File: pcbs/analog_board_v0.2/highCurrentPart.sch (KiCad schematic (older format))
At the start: 36 parts, among them J3 CONN_01X04, P1 CONN_01X03, P2 CONN_01X03, P3 CONN_01X03, Q1 DMP2035U, Q2 TSM2314, Q3 DMP2035U, Q4 TSM2314, Q5 DMP2035U, Q6 TSM2314, Q7 DMP2035U, Q8 TSM2314, Q9 MMBT3904, U3 ICL7660S, U4 AD8616

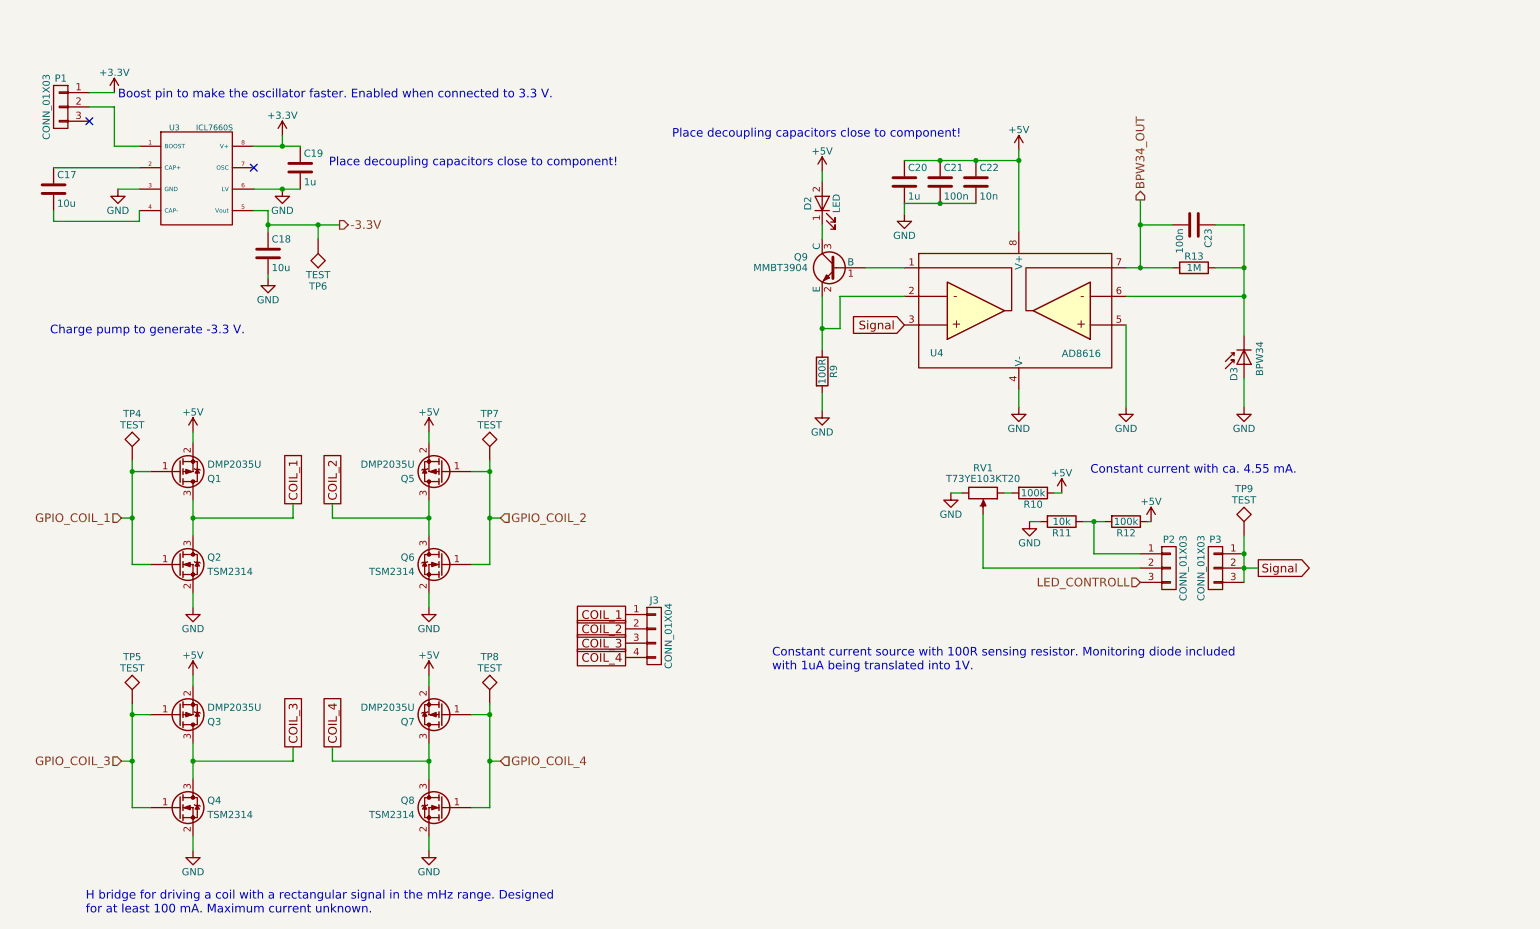
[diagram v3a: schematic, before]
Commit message: Small changes on the backplane standing out.
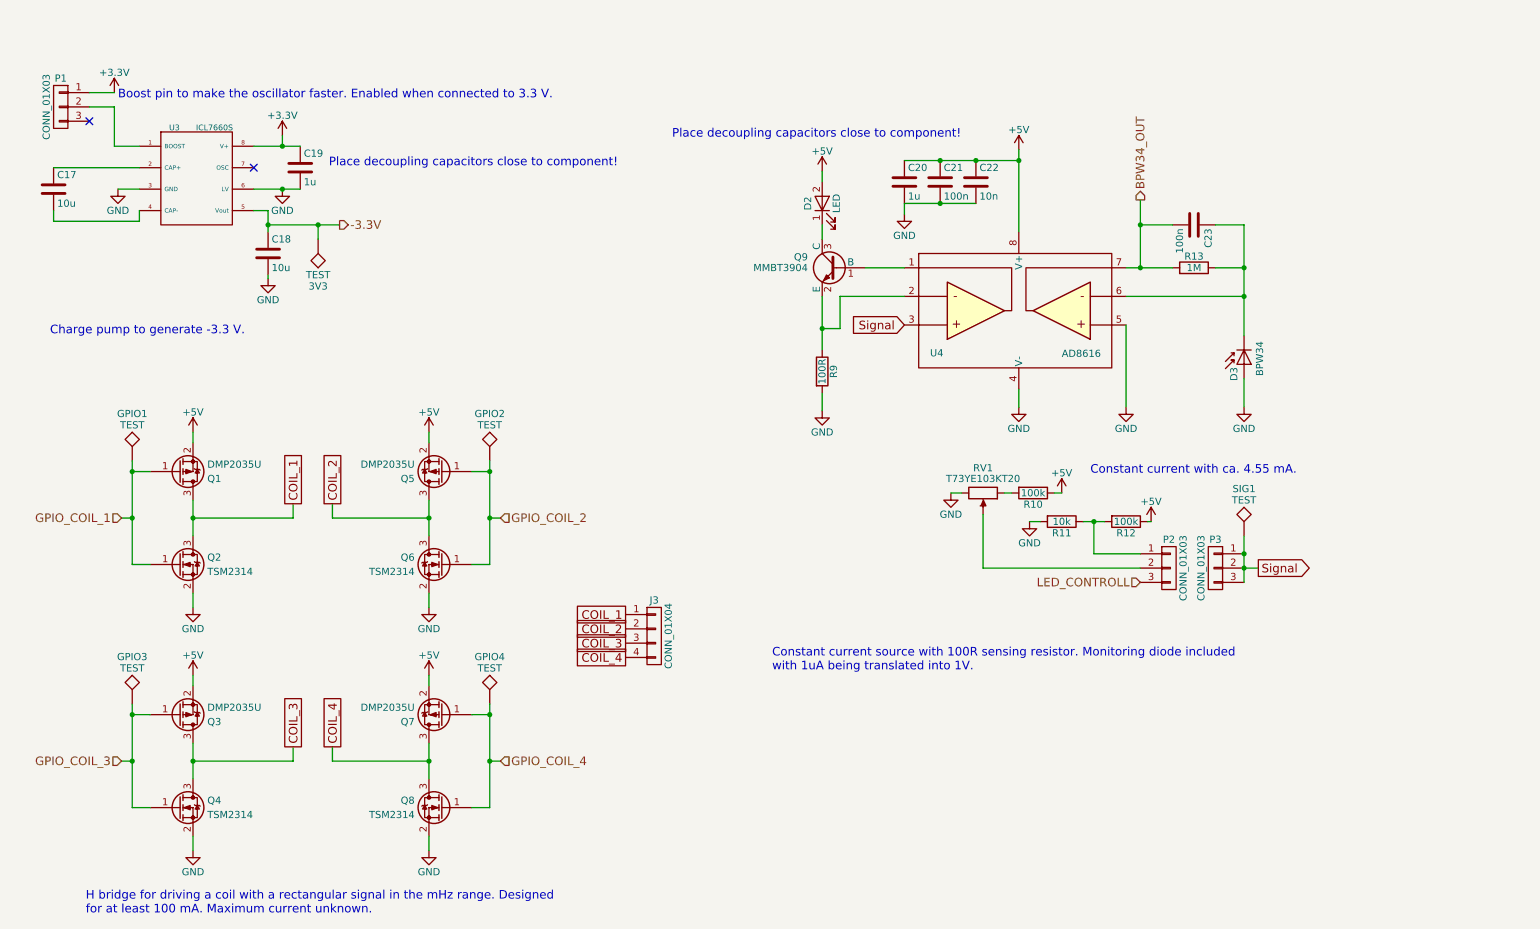
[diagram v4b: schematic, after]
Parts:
- renumbered TP6 to 3V3, TP4 to GPIO1, TP7 to GPIO2, TP5 to GPIO3, TP8 to GPIO4, TP9 to SIG1
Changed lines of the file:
@@
 $EndDescr
 $Comp
-L GND #PWR36
+L GND #PWR018
 U 1 1 5940A4E3
 P 8150 3325
-F 0 "#PWR36" H 8150 3075 50  0001 C CNN
+F 0 "#PWR018" H 8150 3075 50  0001 C CNN
 F 1 "GND" H 8150 3175 50  0000 C CNN
 F 2 "" H 8150 3325 50  0000 C CNN
@@
 $EndComp
 $Comp
-L GND #PWR41
+L GND #PWR019
 U 1 1 5940A554
 P 9725 3325
-F 0 "#PWR41" H 9725 3075 50  0001 C CNN
+F 0 "#PWR019" H 9725 3075 50  0001 C CNN
 F 1 "GND" H 9725 3175 50  0000 C CNN
 F 2 "" H 9725 3325 50  0000 C CNN
@@
 	6775 2050 6775 2150
 $Comp
-L +5V #PWR31
+L +5V #PWR020
 U 1 1 5940A5DC
 P 6775 1675
-F 0 "#PWR31" H 6775 1525 50  0001 C CNN
+F 0 "#PWR020" H 6775 1525 50  0001 C CNN
 F 1 "+5V" H 6775 1815 50  0000 C CNN
 F 2 "" H 6775 1675 50  0000 C CNN
@@
 	6775 1675 6775 1750
 $Comp
-L GND #PWR32
+L GND #PWR021
 U 1 1 5940A5E4
 P 6775 3350
-F 0 "#PWR32" H 6775 3100 50  0001 C CNN
+F 0 "#PWR021" H 6775 3100 50  0001 C CNN
 F 1 "GND" H 6775 3200 50  0000 C CNN
 F 2 "" H 6775 3350 50  0000 C CNN
@@
 Signal
 $Comp
-L GND #PWR34
+L GND #PWR022
 U 1 1 5940A601
 P 7675 3925
-F 0 "#PWR34" H 7675 3675 50  0001 C CNN
+F 0 "#PWR022" H 7675 3675 50  0001 C CNN
 F 1 "GND" H 7675 3775 50  0000 C CNN
 F 2 "" H 7675 3925 50  0000 C CNN
@@
 Signal
 $Comp
-L +5V #PWR38
+L +5V #PWR023
 U 1 1 5940A60A
 P 8450 3925
-F 0 "#PWR38" H 8450 3775 50  0001 C CNN
+F 0 "#PWR023" H 8450 3775 50  0001 C CNN
 F 1 "+5V" H 8450 4065 50  0000 C CNN
 F 2 "" H 8450 3925 50  0000 C CNN
@@
 Connection ~ 6775 2775
 $Comp
-L GND #PWR39
+L GND #PWR024
 U 1 1 5940EF10
 P 8900 3325
-F 0 "#PWR39" H 8900 3075 50  0001 C CNN
+F 0 "#PWR024" H 8900 3075 50  0001 C CNN
 F 1 "GND" H 8900 3175 50  0000 C CNN
 F 2 "" H 8900 3325 50  0000 C CNN
@@
 	8900 2750 8900 3325
 $Comp
-L +5V #PWR35
+L +5V #PWR025
 U 1 1 594122D1
 P 8150 1525
-F 0 "#PWR35" H 8150 1375 50  0001 C CNN
+F 0 "#PWR025" H 8150 1375 50  0001 C CNN
 F 1 "+5V" H 8150 1665 50  0000 C CNN
 F 2 "" H 8150 1525 50  0000 C CNN
@@
 Connection ~ 7600 1600
 $Comp
-L GND #PWR33
+L GND #PWR026
 U 1 1 594122F3
 P 7350 1975
-F 0 "#PWR33" H 7350 1725 50  0001 C CNN
+F 0 "#PWR026" H 7350 1725 50  0001 C CNN
 F 1 "GND" H 7350 1825 50  0000 C CNN
 F 2 "" H 7350 1975 50  0000 C CNN
@@
 	9725 4450 9825 4450
 $Comp
-L TEST TP9
+L TEST SIG1
 U 1 1 594174AB
 P 9725 4225
-F 0 "TP9" H 9725 4525 50  0000 C BNN
+F 0 "SIG1" H 9725 4525 50  0000 C BNN
 F 1 "TEST" H 9725 4475 50  0000 C CNN
 F 2 "Tespoints:TP_SMD_quadr_1mm" H 9725 4225 50  0001 C CNN
@@
 $EndComp
 $Comp
-L +5V #PWR40
+L +5V #PWR027
 U 1 1 5941842E
 P 9075 4125
-F 0 "#PWR40" H 9075 3975 50  0001 C CNN
+F 0 "#PWR027" H 9075 3975 50  0001 C CNN
 F 1 "+5V" H 9075 4265 50  0000 C CNN
 F 2 "" H 9075 4125 50  0000 C CNN
@@
 	8600 4125 8750 4125
 $Comp
-L GND #PWR37
+L GND #PWR028
 U 1 1 5941869D
 P 8225 4125
-F 0 "#PWR37" H 8225 3875 50  0001 C CNN
+F 0 "#PWR028" H 8225 3875 50  0001 C CNN
 F 1 "GND" H 8225 3975 50  0000 C CNN
 F 2 "" H 8225 4125 50  0000 C CNN
@@
 BPW34_OUT
 $Comp
-L GND #PWR26
+L GND #PWR029
 U 1 1 59553CC6
 P 3000 1800
-F 0 "#PWR26" H 3000 1550 50  0001 C CNN
+F 0 "#PWR029" H 3000 1550 50  0001 C CNN
 F 1 "GND" H 3000 1650 50  0000 C CNN
 F 2 "" H 3000 1800 50  0001 C CNN
@@
 	2375 5675 2375 5925
 $Comp
-L GND #PWR23
+L GND #PWR030
 U 1 1 59557860
 P 2375 6425
-F 0 "#PWR23" H 2375 6175 50  0001 C CNN
+F 0 "#PWR030" H 2375 6175 50  0001 C CNN
 F 1 "GND" H 2375 6275 50  0000 C CNN
 F 2 "" H 2375 6425 50  0000 C CNN
@@
 	2375 6325 2375 6425
 $Comp
-L +5V #PWR22
+L +5V #PWR031
 U 1 1 59557DF9
 P 2375 5200
-F 0 "#PWR22" H 2375 5050 50  0001 C CNN
+F 0 "#PWR031" H 2375 5050 50  0001 C CNN
 F 1 "+5V" H 2375 5340 50  0000 C CNN
 F 2 "" H 2375 5200 50  0000 C CNN
@@
 	4025 5675 4025 5925
 $Comp
-L GND #PWR30
+L GND #PWR032
 U 1 1 59558304
 P 4025 6425
-F 0 "#PWR30" H 4025 6175 50  0001 C CNN
+F 0 "#PWR032" H 4025 6175 50  0001 C CNN
 F 1 "GND" H 4025 6275 50  0000 C CNN
 F 2 "" H 4025 6425 50  0000 C CNN
@@
 	4025 6325 4025 6425
 $Comp
-L +5V #PWR29
+L +5V #PWR033
 U 1 1 5955830B
 P 4025 5200
-F 0 "#PWR29" H 4025 5050 50  0001 C CNN
+F 0 "#PWR033" H 4025 5050 50  0001 C CNN
 F 1 "+5V" H 4025 5340 50  0000 C CNN
 F 2 "" H 4025 5200 50  0000 C CNN
@@
 	2375 3975 2375 4225
 $Comp
-L GND #PWR21
+L GND #PWR034
 U 1 1 5956291A
 P 2375 4725
-F 0 "#PWR21" H 2375 4475 50  0001 C CNN
+F 0 "#PWR034" H 2375 4475 50  0001 C CNN
 F 1 "GND" H 2375 4575 50  0000 C CNN
 F 2 "" H 2375 4725 50  0000 C CNN
@@
 	2375 4625 2375 4725
 $Comp
-L +5V #PWR20
+L +5V #PWR035
 U 1 1 59562921
 P 2375 3500
-F 0 "#PWR20" H 2375 3350 50  0001 C CNN
+F 0 "#PWR035" H 2375 3350 50  0001 C CNN
 F 1 "+5V" H 2375 3640 50  0000 C CNN
 F 2 "" H 2375 3500 50  0000 C CNN
@@
 	4025 3975 4025 4225
 $Comp
-L GND #PWR28
+L GND #PWR036
 U 1 1 59562931
 P 4025 4725
-F 0 "#PWR28" H 4025 4475 50  0001 C CNN
+F 0 "#PWR036" H 4025 4475 50  0001 C CNN
 F 1 "GND" H 4025 4575 50  0000 C CNN
 F 2 "" H 4025 4725 50  0000 C CNN
@@
 	4025 4625 4025 4725
 $Comp
-L +5V #PWR27
+L +5V #PWR037
 U 1 1 59562938
 P 4025 3500
-F 0 "#PWR27" H 4025 3350 50  0001 C CNN
+F 0 "#PWR037" H 4025 3350 50  0001 C CNN
 F 1 "+5V" H 4025 3640 50  0000 C CNN
 F 2 "" H 4025 3500 50  0000 C CNN
@@
 LED_CONTROLL
 $Comp
-L GND #PWR19
+L GND #PWR038
 U 1 1 59563916
 P 1850 1800
-F 0 "#PWR19" H 1850 1550 50  0001 C CNN
+F 0 "#PWR038" H 1850 1550 50  0001 C CNN
 F 1 "GND" H 1850 1650 50  0000 C CNN
 F 2 "" H 1850 1800 50  0001 C CNN
@@
 	2000 2025 2000 1950
 $Comp
-L +3.3V #PWR25
+L +3.3V #PWR039
 U 1 1 59563EC0
 P 3000 1425
-F 0 "#PWR25" H 3000 1275 50  0001 C CNN
+F 0 "#PWR039" H 3000 1275 50  0001 C CNN
 F 1 "+3.3V" H 3000 1565 50  0000 C CNN
 F 2 "" H 3000 1425 50  0001 C CNN
@@
 	2900 1950 2900 2100
 $Comp
-L GND #PWR24
+L GND #PWR040
 U 1 1 5956469D
 P 2900 2425
-F 0 "#PWR24" H 2900 2175 50  0001 C CNN
+F 0 "#PWR040" H 2900 2175 50  0001 C CNN
 F 1 "GND" H 2900 2275 50  0000 C CNN
 F 2 "" H 2900 2425 50  0001 C CNN
@@
 $EndComp
 $Comp
-L +3.3V #PWR18
+L +3.3V #PWR041
 U 1 1 595680C2
 P 1825 1125
-F 0 "#PWR18" H 1825 975 50  0001 C CNN
+F 0 "#PWR041" H 1825 975 50  0001 C CNN
 F 1 "+3.3V" H 1825 1265 50  0000 C CNN
 F 2 "" H 1825 1125 50  0001 C CNN
@@
 COIL_4
 $Comp
-L TEST TP4
+L TEST GPIO1
 U 1 1 59595C55
 P 1950 3700
-F 0 "TP4" H 1950 4000 50  0000 C BNN
+F 0 "GPIO1" H 1950 4000 50  0000 C BNN
 F 1 "TEST" H 1950 3950 50  0000 C CNN
 F 2 "Tespoints:TP_SMD_quadr_1mm" H 1950 3700 50  0001 C CNN
@@
 $EndComp
 $Comp
-L TEST TP7
+L TEST GPIO2
 U 1 1 59596119
 P 4450 3700
-F 0 "TP7" H 4450 4000 50  0000 C BNN
+F 0 "GPIO2" H 4450 4000 50  0000 C BNN
 F 1 "TEST" H 4450 3950 50  0000 C CNN
 F 2 "Tespoints:TP_SMD_quadr_1mm" H 4450 3700 50  0001 C CNN
@@
 $EndComp
 $Comp
-L TEST TP5
+L TEST GPIO3
 U 1 1 59596260
 P 1950 5400
-F 0 "TP5" H 1950 5700 50  0000 C BNN
+F 0 "GPIO3" H 1950 5700 50  0000 C BNN
 F 1 "TEST" H 1950 5650 50  0000 C CNN
 F 2 "Tespoints:TP_SMD_quadr_1mm" H 1950 5400 50  0001 C CNN
@@
 $EndComp
 $Comp
-L TEST TP8
+L TEST GPIO4
 U 1 1 5959632C
 P 4450 5400
-F 0 "TP8" H 4450 5700 50  0000 C BNN
+F 0 "GPIO4" H 4450 5700 50  0000 C BNN
 F 1 "TEST" H 4450 5650 50  0000 C CNN
 F 2 "Tespoints:TP_SMD_quadr_1mm" H 4450 5400 50  0001 C CNN
@@
 $EndComp
 $Comp
-L TEST TP6
+L TEST 3V3
 U 1 1 59596507
 P 3250 2150
-F 0 "TP6" H 3250 2450 50  0000 C BNN
+F 0 "3V3" H 3250 2450 50  0000 C BNN
 F 1 "TEST" H 3250 2400 50  0000 C CNN
 F 2 "Tespoints:TP_SMD_quadr_1mm" H 3250 2150 50  0001 C CNN

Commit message: Backplane definitely finished. Somethings wrong with TIA. Has to be checked tomorrow.
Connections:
- net +3V3: now also C20.1, C21.1, C22.1, U4.8 (V+)
- net +5V: no longer C20.1, C21.1, C22.1, U4.8 (V+)
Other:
- note added: "Low-pass has a cut-off freq. of approx. 1.6 Hz, ergo DC."
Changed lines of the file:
@@
 	8900 2750 8900 3325
-$Comp
-L +5V #PWR025
-U 1 1 594122D1
-P 8150 1525
-F 0 "#PWR025" H 8150 1375 50  0001 C CNN
-F 1 "+5V" H 8150 1665 50  0000 C CNN
-F 2 "" H 8150 1525 50  0000 C CNN
-F 3 "" H 8150 1525 50  0000 C CNN
-	1    8150 1525
-	1    0    0    -1
-$EndComp
 $Comp
 L C C20
@@
 Connection ~ 7600 1600
 $Comp
-L GND #PWR026
+L GND #PWR025
 U 1 1 594122F3
 P 7350 1975
-F 0 "#PWR026" H 7350 1725 50  0001 C CNN
+F 0 "#PWR025" H 7350 1725 50  0001 C CNN
 F 1 "GND" H 7350 1825 50  0000 C CNN
 F 2 "" H 7350 1975 50  0000 C CNN
@@
 $EndComp
 $Comp
-L +5V #PWR027
+L +5V #PWR026
 U 1 1 5941842E
 P 9075 4125
-F 0 "#PWR027" H 9075 3975 50  0001 C CNN
+F 0 "#PWR026" H 9075 3975 50  0001 C CNN
 F 1 "+5V" H 9075 4265 50  0000 C CNN
 F 2 "" H 9075 4125 50  0000 C CNN
@@
 	8600 4125 8750 4125
 $Comp
-L GND #PWR028
+L GND #PWR027
 U 1 1 5941869D
 P 8225 4125
-F 0 "#PWR028" H 8225 3875 50  0001 C CNN
+F 0 "#PWR027" H 8225 3875 50  0001 C CNN
 F 1 "GND" H 8225 3975 50  0000 C CNN
 F 2 "" H 8225 4125 50  0000 C CNN
@@
 BPW34_OUT
 $Comp
-L GND #PWR029
+L GND #PWR028
 U 1 1 59553CC6
 P 3000 1800
-F 0 "#PWR029" H 3000 1550 50  0001 C CNN
+F 0 "#PWR028" H 3000 1550 50  0001 C CNN
 F 1 "GND" H 3000 1650 50  0000 C CNN
 F 2 "" H 3000 1800 50  0001 C CNN
@@
 	2375 5675 2375 5925
 $Comp
-L GND #PWR030
+L GND #PWR029
 U 1 1 59557860
 P 2375 6425
-F 0 "#PWR030" H 2375 6175 50  0001 C CNN
+F 0 "#PWR029" H 2375 6175 50  0001 C CNN
 F 1 "GND" H 2375 6275 50  0000 C CNN
 F 2 "" H 2375 6425 50  0000 C CNN
@@
 	2375 6325 2375 6425
 $Comp
-L +5V #PWR031
+L +5V #PWR030
 U 1 1 59557DF9
 P 2375 5200
-F 0 "#PWR031" H 2375 5050 50  0001 C CNN
+F 0 "#PWR030" H 2375 5050 50  0001 C CNN
 F 1 "+5V" H 2375 5340 50  0000 C CNN
 F 2 "" H 2375 5200 50  0000 C CNN
@@
 	4025 5675 4025 5925
 $Comp
-L GND #PWR032
+L GND #PWR031
 U 1 1 59558304
 P 4025 6425
-F 0 "#PWR032" H 4025 6175 50  0001 C CNN
+F 0 "#PWR031" H 4025 6175 50  0001 C CNN
 F 1 "GND" H 4025 6275 50  0000 C CNN
 F 2 "" H 4025 6425 50  0000 C CNN
@@
 	4025 6325 4025 6425
 $Comp
-L +5V #PWR033
+L +5V #PWR032
 U 1 1 5955830B
 P 4025 5200
-F 0 "#PWR033" H 4025 5050 50  0001 C CNN
+F 0 "#PWR032" H 4025 5050 50  0001 C CNN
 F 1 "+5V" H 4025 5340 50  0000 C CNN
 F 2 "" H 4025 5200 50  0000 C CNN
@@
 	2375 3975 2375 4225
 $Comp
-L GND #PWR034
+L GND #PWR033
 U 1 1 5956291A
 P 2375 4725
-F 0 "#PWR034" H 2375 4475 50  0001 C CNN
+F 0 "#PWR033" H 2375 4475 50  0001 C CNN
 F 1 "GND" H 2375 4575 50  0000 C CNN
 F 2 "" H 2375 4725 50  0000 C CNN
@@
 	2375 4625 2375 4725
 $Comp
-L +5V #PWR035
+L +5V #PWR034
 U 1 1 59562921
 P 2375 3500
-F 0 "#PWR035" H 2375 3350 50  0001 C CNN
+F 0 "#PWR034" H 2375 3350 50  0001 C CNN
 F 1 "+5V" H 2375 3640 50  0000 C CNN
 F 2 "" H 2375 3500 50  0000 C CNN
@@
 	4025 3975 4025 4225
 $Comp
-L GND #PWR036
+L GND #PWR035
 U 1 1 59562931
 P 4025 4725
-F 0 "#PWR036" H 4025 4475 50  0001 C CNN
+F 0 "#PWR035" H 4025 4475 50  0001 C CNN
 F 1 "GND" H 4025 4575 50  0000 C CNN
 F 2 "" H 4025 4725 50  0000 C CNN
@@
 	4025 4625 4025 4725
 $Comp
-L +5V #PWR037
+L +5V #PWR036
 U 1 1 59562938
 P 4025 3500
-F 0 "#PWR037" H 4025 3350 50  0001 C CNN
+F 0 "#PWR036" H 4025 3350 50  0001 C CNN
 F 1 "+5V" H 4025 3640 50  0000 C CNN
 F 2 "" H 4025 3500 50  0000 C CNN
@@
 LED_CONTROLL
 $Comp
-L GND #PWR038
+L GND #PWR037
 U 1 1 59563916
 P 1850 1800
-F 0 "#PWR038" H 1850 1550 50  0001 C CNN
+F 0 "#PWR037" H 1850 1550 50  0001 C CNN
 F 1 "GND" H 1850 1650 50  0000 C CNN
 F 2 "" H 1850 1800 50  0001 C CNN
@@
 	2000 2025 2000 1950
 $Comp
-L +3.3V #PWR039
+L +3.3V #PWR038
 U 1 1 59563EC0
 P 3000 1425
-F 0 "#PWR039" H 3000 1275 50  0001 C CNN
+F 0 "#PWR038" H 3000 1275 50  0001 C CNN
 F 1 "+3.3V" H 3000 1565 50  0000 C CNN
 F 2 "" H 3000 1425 50  0001 C CNN
@@
 	2900 1950 2900 2100
 $Comp
-L GND #PWR040
+L GND #PWR039
 U 1 1 5956469D
 P 2900 2425
-F 0 "#PWR040" H 2900 2175 50  0001 C CNN
+F 0 "#PWR039" H 2900 2175 50  0001 C CNN
 F 1 "GND" H 2900 2275 50  0000 C CNN
 F 2 "" H 2900 2425 50  0001 C CNN
@@
 $EndComp
 $Comp
-L +3.3V #PWR041
+L +3.3V #PWR040
 U 1 1 595680C2
 P 1825 1125
-F 0 "#PWR041" H 1825 975 50  0001 C CNN
+F 0 "#PWR040" H 1825 975 50  0001 C CNN
 F 1 "+3.3V" H 1825 1265 50  0000 C CNN
 F 2 "" H 1825 1125 50  0001 C CNN
@@
 Wire Wire Line
 	1825 1500 2000 1500
+Text Notes 8325 1200 0    60   ~ 0
+Low-pass has a cut-off freq. of approx. 1.6 Hz, ergo DC.
+$Comp
+L +3.3V #PWR041
+U 1 1 595BE0DA
+P 8150 1525
+F 0 "#PWR041" H 8150 1375 50  0001 C CNN
+F 1 "+3.3V" H 8150 1665 50  0000 C CNN
+F 2 "" H 8150 1525 50  0001 C CNN
+F 3 "" H 8150 1525 50  0001 C CNN
+	1    8150 1525
+	-1   0    0    -1
+$EndComp
 $EndSCHEMATC
